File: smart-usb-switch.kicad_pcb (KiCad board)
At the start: 2 copper layers, 50.8 x 20.3 mm, 8 parts, among them J1 USB_A, J2 USB_A, J3 Conn_01x04, J4 Conn_01x02, Q1 2N7002E, U1 ESP-12F, U2 TLV75533PDBV

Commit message: Add buttons. Reroute, improve docs
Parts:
- added SW1: SW_Push, Button_Switch_SMD:SW_SPST_SKQG_WithStem, B.Cu at (137.2, 94.0)
- added SW2: SW_Push, Button_Switch_SMD:SW_SPST_SKQG_WithStem, B.Cu at (125.7, 94.0)
- Q1: value 2N7002E -> DMN6140L-13
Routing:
- net Net-(SW1-Pad1): track 0.00 -> 23.1 mm, vias 0 -> 1
- net GND: track 68.1 -> 83.6 mm, vias 1 -> 3
- net Net-(SW2-Pad1): track 0.00 -> 12.6 mm, vias 0 -> 1
- net +3V3: track 57.8 -> 46.4 mm, vias 0 -> 1
- net VBUS: track 61.1 -> 67.7 mm
- net Net-(J3-Pad3): track 15.5 -> 22.0 mm
- net Net-(J3-Pad4): track 17.3 -> 13.6 mm
- net Net-(J4-Pad2): track 25.1 -> 26.4 mm
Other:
- board text added: "Buttons: GPIO12/13 (D6/D7)"
- board text added: "PROG"
- board text added: "USB power: GPIO4 (D2)"
- board text removed: "FLASH"
- board text removed: "GPIO 4 controls USB power"

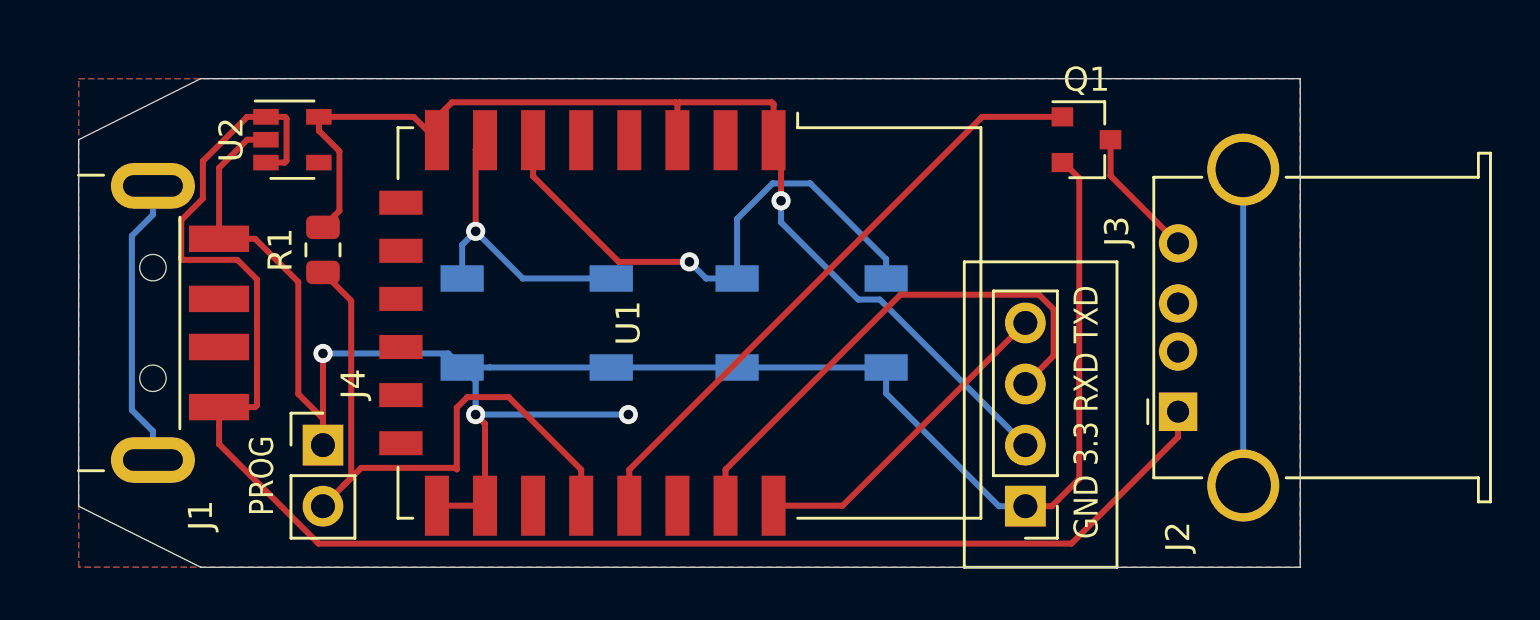
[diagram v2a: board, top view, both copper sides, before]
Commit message: Make board narrower so it's more likely to fit in side-by-side USB ports
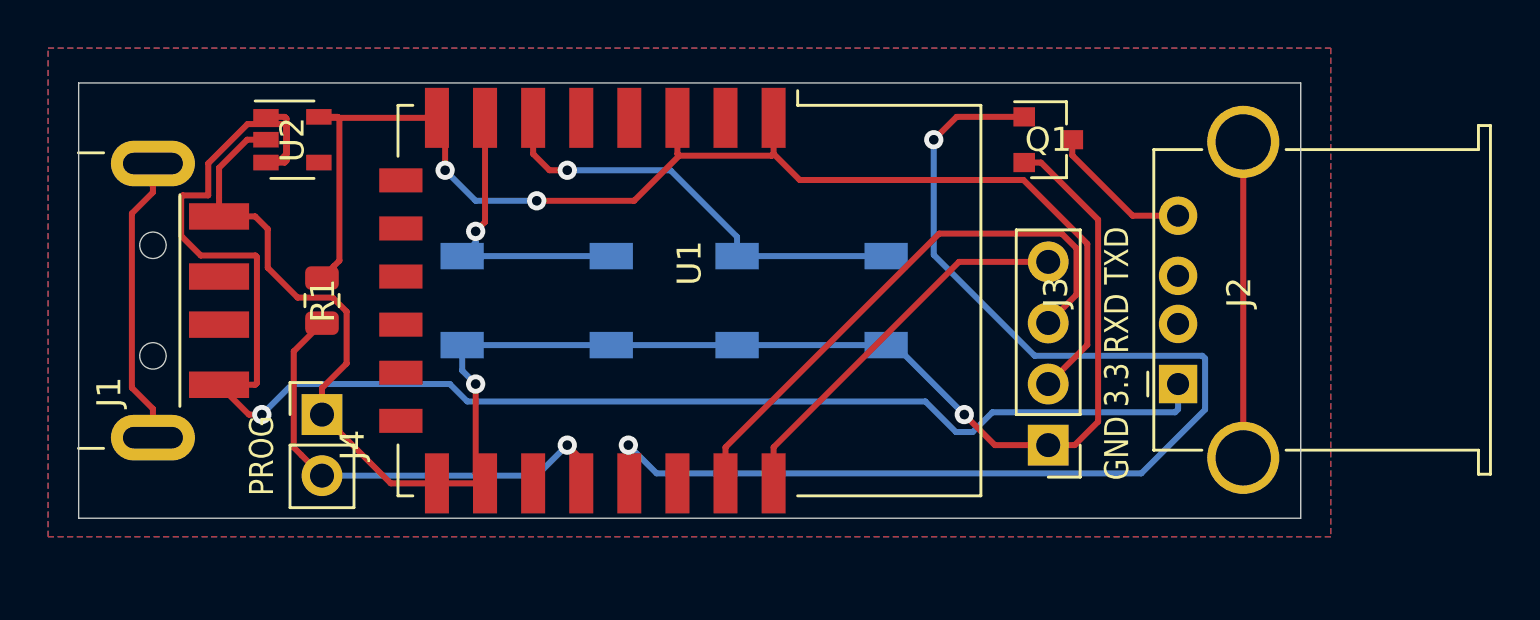
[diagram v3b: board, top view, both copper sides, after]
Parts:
- moved J3 2.71 mm to (147.0, 99.1)
- moved R1 2.11 mm to (116.8, 93.0)
- moved Q1 1.59 mm to (147.0, 86.4)
- moved J4 1.27 mm to (116.8, 97.8)
- moved J2 1.15 mm to (152.4, 96.5)
- moved J1 0.93 mm to (102.9, 93.0)
- moved SW1 0.93 mm to (137.2, 93.0)
- moved SW2 0.93 mm to (125.7, 93.0)
- moved U1 0.93 mm to (132.1, 93.0)
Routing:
- net Net-(Q1-Pad1): track 25.6 -> 51.3 mm, vias 0 -> 2
- net GND: track 83.6 -> 72.2 mm, vias 3 -> 2
- net +3V3: track 46.4 -> 54.3 mm, vias 1 -> 2
- net Net-(J4-Pad2): track 26.4 -> 19.9 mm, vias 0 -> 1
- net Net-(SW1-Pad1): track 23.1 -> 18.4 mm
- net Net-(J3-Pad4): track 13.6 -> 16.1 mm
- net Net-(J3-Pad3): track 22.0 -> 23.6 mm
- net Net-(J2-Pad4): track 5.47 -> 6.09 mm
- net VBUS: track 67.7 -> 67.3 mm, vias 0 -> 1
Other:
- board size 50.8 x 20.3 mm -> 50.8 x 18.1 mm

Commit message: re-route with freerouting.org
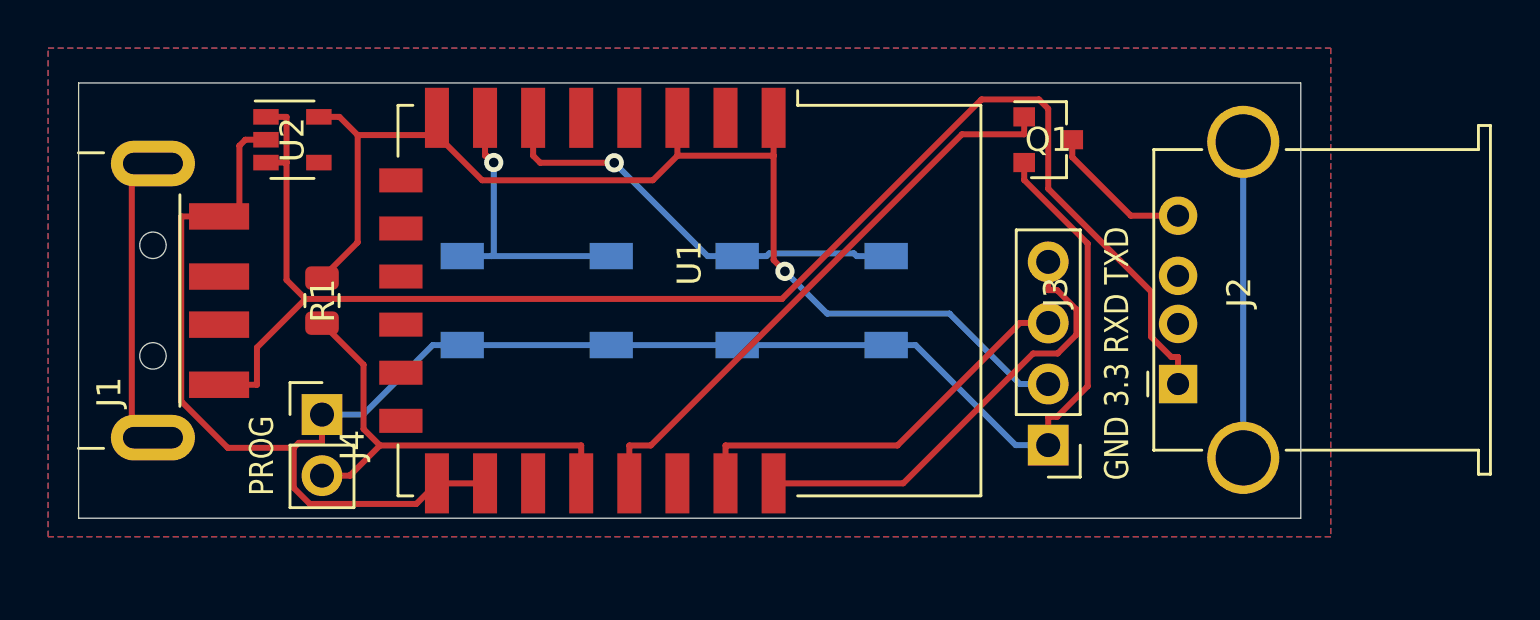
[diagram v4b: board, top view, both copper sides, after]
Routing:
- net Net-(Q1-Pad1): track 51.3 -> 24.1 mm, vias 2 -> 0
- net GND: track 72.2 -> 79.3 mm, vias 2 -> 0
- net Net-(J3-Pad3): track 23.6 -> 17.1 mm
- net +3V3: track 54.3 -> 48.7 mm, vias 2 -> 1
- net VBUS: track 67.3 -> 63.9 mm, vias 1 -> 0
- net Net-(J3-Pad4): track 16.1 -> 18.9 mm
- net Net-(J4-Pad2): track 19.9 -> 19.0 mm, vias 1 -> 0

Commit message: JLCPCB mfg
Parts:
- U2: value TLV75533PDBV -> MIC5219-3.3YM5-TR
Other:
- board text added: "v1"
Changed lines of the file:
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@@
-(kicad_pcb (version 20171130) (host pcbnew 5.1.5-52549c5~84~ubuntu18.04.1)
+(kicad_pcb (version 20171130) (host pcbnew 5.1.5-52549c5~84~ubuntu19.10.1)
   (general
     (thickness 1.6)
-    (drawings 11)
+    (drawings 12)
     (tracks 119)
     (zones 0)
@@
       (drillshape 0)
       (scaleselection 1)
-      (outputdirectory "../../Desktop/"))
+      (outputdirectory "mfg/jlcpcb.com/v1/"))
   )
   (net 0 "")
@@
       (effects (font (size 1 1) (thickness 0.15)))
     )
-    (fp_text value TLV75533PDBV (at 0 2.9) (layer F.Fab)
+    (fp_text value MIC5219-3.3YM5-TR (at 0 2.9) (layer F.Fab)
       (effects (font (size 1 1) (thickness 0.15)))
     )
@@
     )
   )
+  (gr_text v1 (at 111.76 100.33) (layer F.SilkS)
+    (effects (font (size 0.5 0.5) (thickness 0.125)))
+  )
   (gr_line (start 157.5 102.1) (end 106.68 102.1) (layer Edge.Cuts) (width 0.05))
